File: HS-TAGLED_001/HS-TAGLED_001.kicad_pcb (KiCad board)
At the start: 2 copper layers, 95 x 95 mm, 14 parts, among them J2 Conn_01x03, U1 TSOP59540TR1

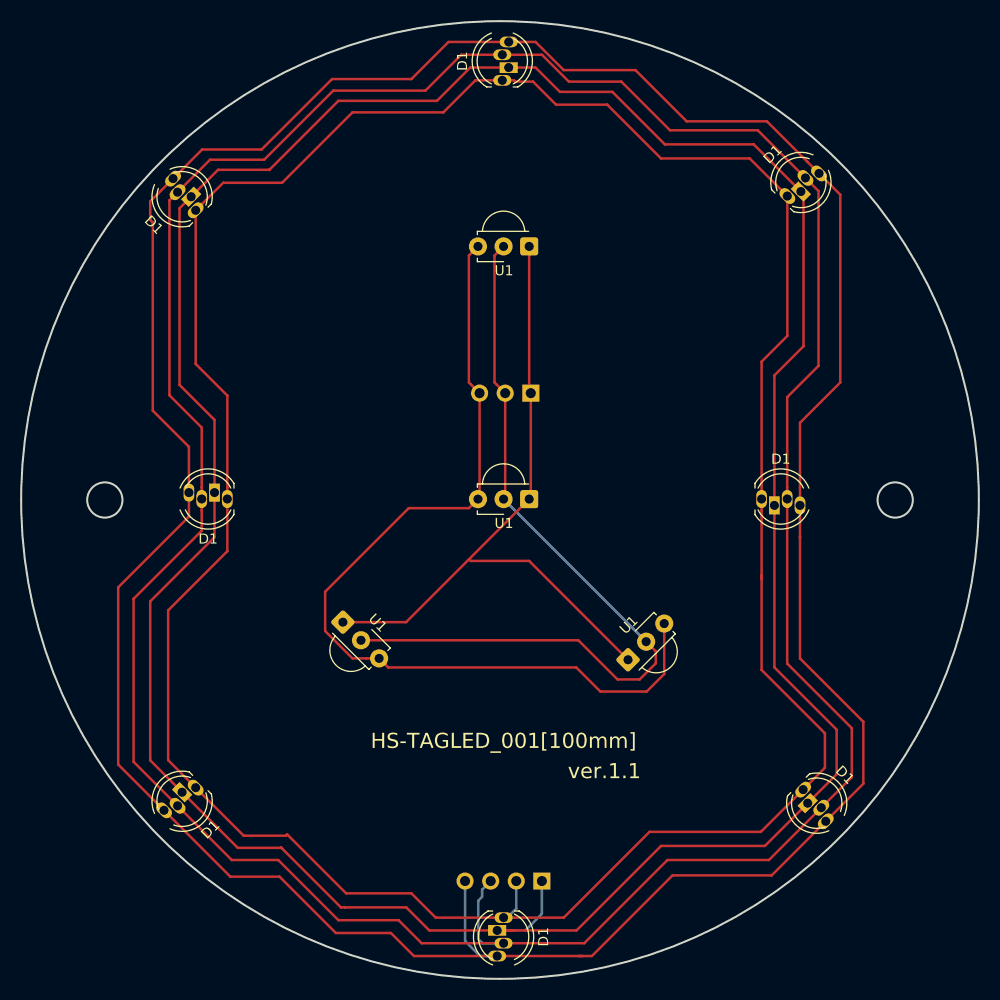
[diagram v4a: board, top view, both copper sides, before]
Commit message: ・LEDの位置変更
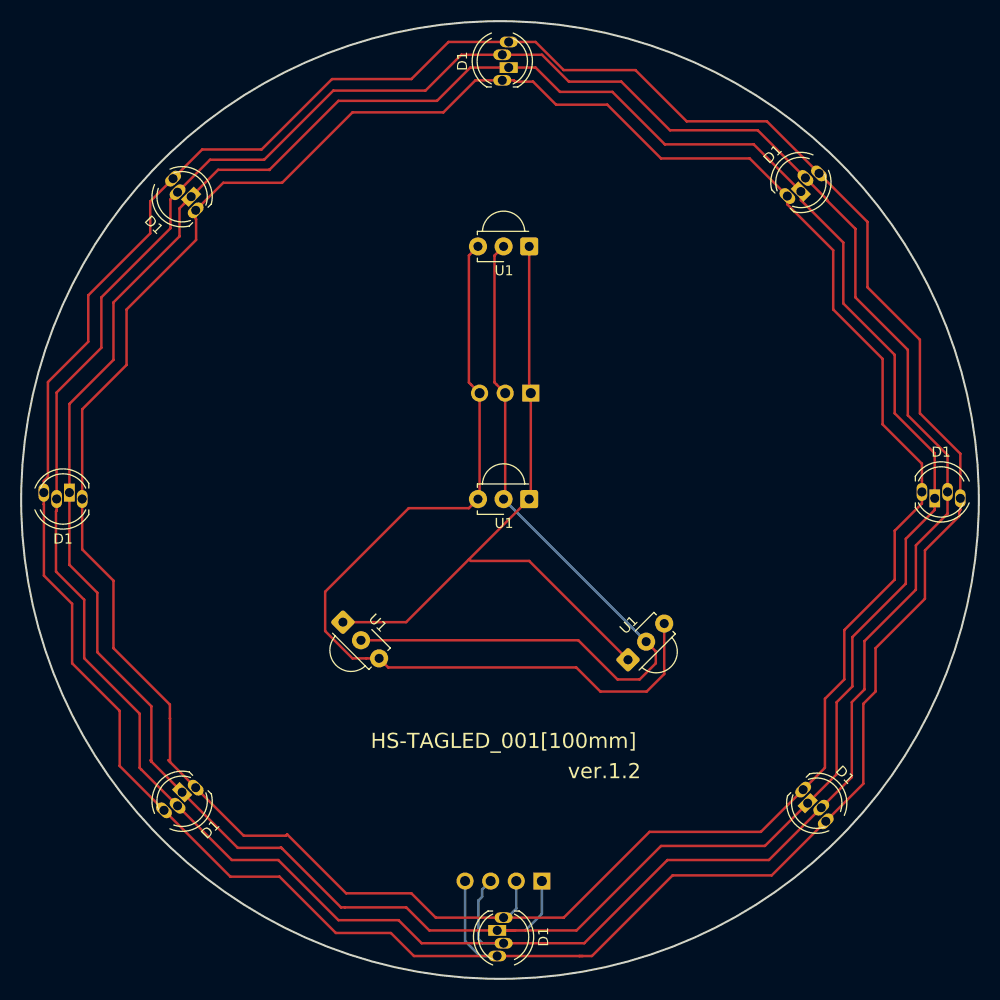
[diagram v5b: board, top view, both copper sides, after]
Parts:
- moved D1 15.9 mm to (171.5, 89.3)
- moved D1 14.4 mm to (88.2, 90.0)
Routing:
- net Net-(D1-Pad1): track 284.1 -> 295.1 mm
- net Net-(D1-Pad2): track 270.4 -> 280.7 mm
- net Net-(D1-Pad3): track 292.3 -> 301.4 mm
- net Net-(D1-Pad4): track 303.8 -> 311.3 mm
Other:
- outline, holes or cut-outs redrawn
- board text added: "ver.1.2"
- board text removed: "ver.1.1"
